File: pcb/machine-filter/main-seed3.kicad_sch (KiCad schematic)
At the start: 10 parts, among them J14 EXPANSION 2x4, J15 TF-01A

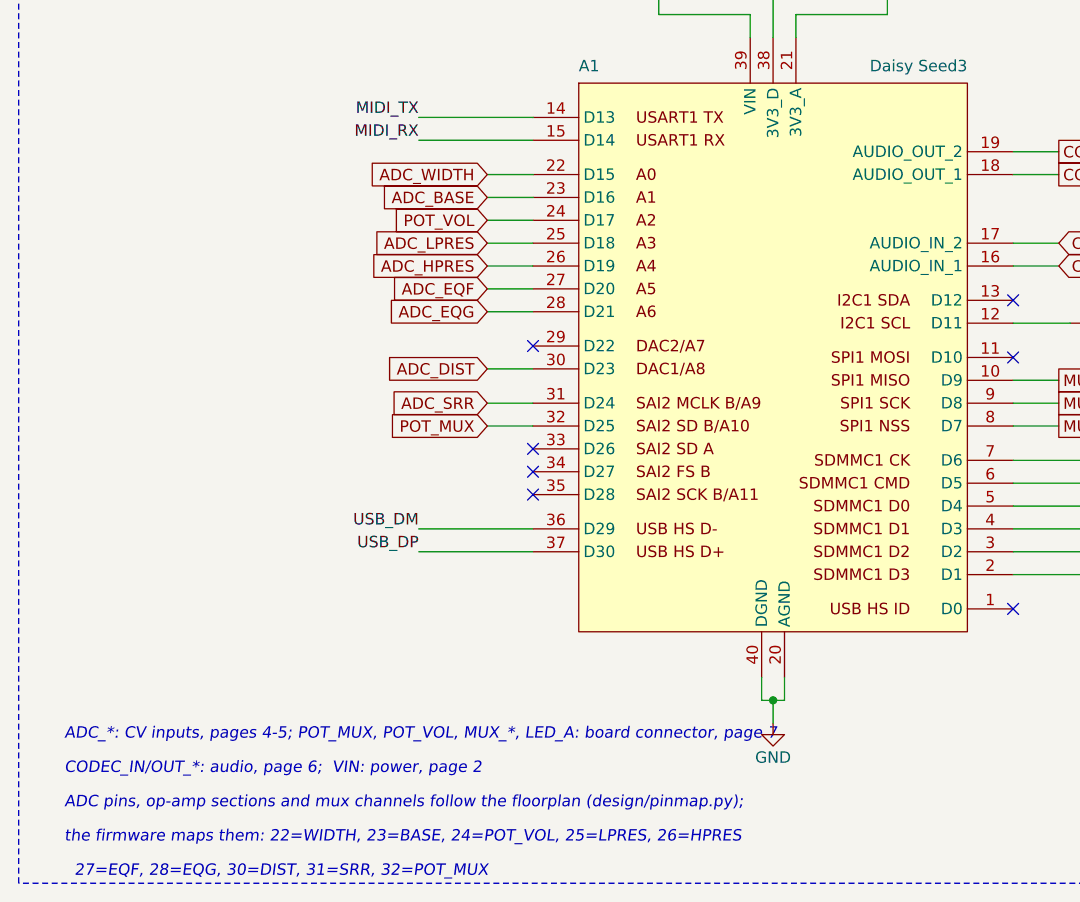
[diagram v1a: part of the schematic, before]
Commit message: Placement step 4: U1 and its CV group; ADC pins re-matched to the placed chips
Re-match pending d's OK (d questioned doing it now): tools/rematch_adc.py,
pinmap ADC_UNIT/SEED_ADC, schematic rebuilt, firmware and placement docs
updated, PCB pads reassigned (U1 re-added: its unit A moved sheets).
WIDTH trace not drawn yet.

Co-Authored-By: Claude Opus 5.5 <noreply@anthropic.com>
Claude-Session: https://claude.ai/code/session_01Cf5qNBi3oNHhbCjPHvswth
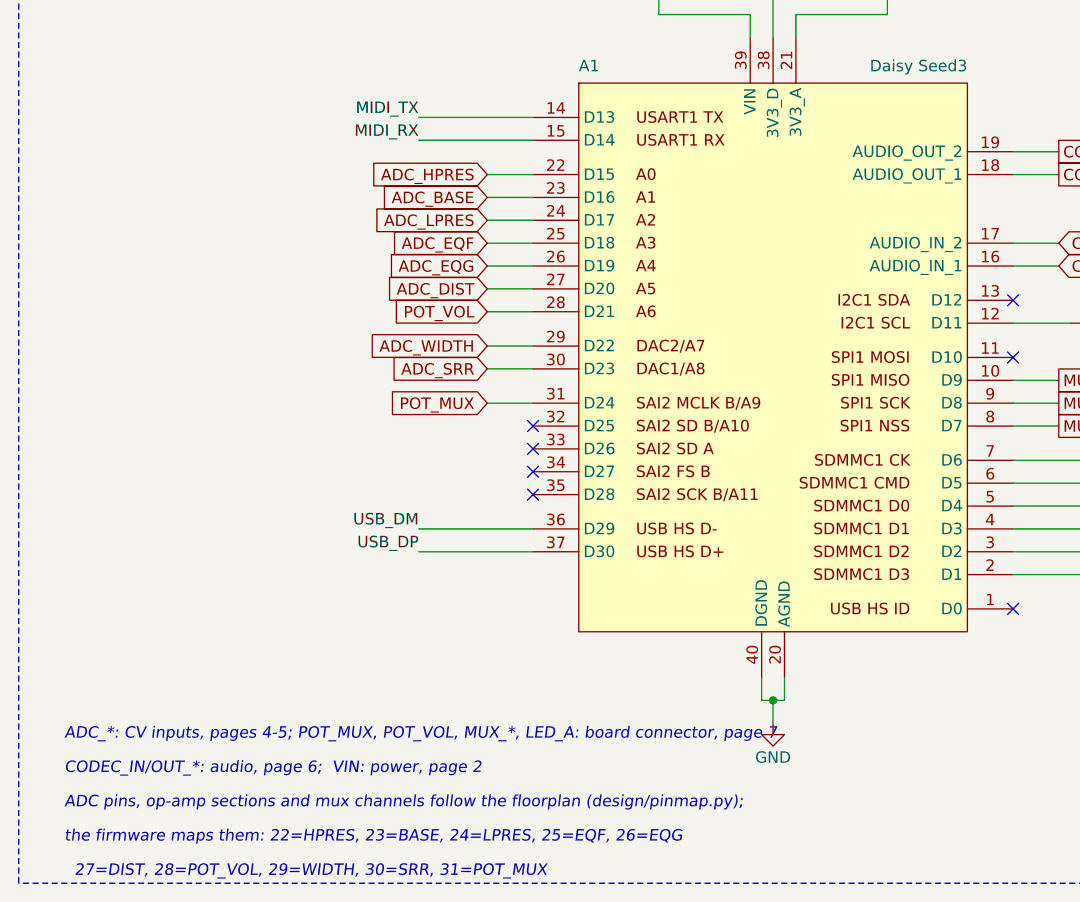
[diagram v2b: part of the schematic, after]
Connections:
- net ADC_DIST: now also A1.27 (D20); no longer A1.30 (D23)
- net ADC_EQF: now also A1.25 (D18); no longer A1.27 (D20)
- net ADC_EQG: now also A1.26 (D19); no longer A1.28 (D21)
- net ADC_HPRES: now also A1.22 (D15); no longer A1.26 (D19)
- net ADC_LPRES: now also A1.24 (D17); no longer A1.25 (D18)
- net ADC_SRR: now also A1.30 (D23); no longer A1.31 (D24)
- net ADC_WIDTH: now also A1.29 (D22); no longer A1.22 (D15)
- net POT_MUX: now also A1.31 (D24); no longer A1.32 (D25)
- net POT_VOL: now also A1.28 (D21); no longer A1.24 (D17)
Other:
- note added: "27=DIST, 28=POT_VOL, 29=WIDTH, 30=SRR, 31=POT_MUX"
- note added: "the firmware maps them: 22=HPRES, 23=BASE, 24=LPRES, 25=EQF, 26=EQG"
- note removed: "27=EQF, 28=EQG, 30=DIST, 31=SRR, 32=POT_MUX"
- note removed: "the firmware maps them: 22=WIDTH, 23=BASE, 24=POT_VOL, 25=LPRES, 26=HPRES"
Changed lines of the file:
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@@
 	)
 	(no_connect
-		(at 72.39 100.33)
+		(at 72.39 109.22)
 	)
 	(no_connect
@@
 		)
 	)
-	(global_label "ADC_WIDTH"
+	(global_label "ADC_HPRES"
 		(shape input)
 		(at 67.31 81.28 180)
@@
 		)
 	)
-	(global_label "POT_VOL"
+	(global_label "ADC_LPRES"
 		(shape input)
 		(at 67.31 86.36 180)
@@
 		)
 	)
-	(global_label "ADC_LPRES"
+	(global_label "ADC_EQF"
 		(shape input)
 		(at 67.31 88.9 180)
@@
 		)
 	)
-	(global_label "ADC_HPRES"
+	(global_label "ADC_EQG"
 		(shape input)
 		(at 67.31 91.44 180)
@@
 		)
 	)
-	(global_label "ADC_EQF"
+	(global_label "ADC_DIST"
 		(shape input)
 		(at 67.31 93.98 180)
@@
 		)
 	)
-	(global_label "ADC_EQG"
+	(global_label "POT_VOL"
 		(shape input)
 		(at 67.31 96.52 180)
@@
 		)
 	)
-	(global_label "ADC_DIST"
+	(global_label "ADC_WIDTH"
+		(shape input)
+		(at 67.31 100.33 180)
+		(fields_autoplaced yes)
+		(effects
+			(font
+				(size 1.27 1.27)
+			)
+			(justify right)
+		)
+		(property "Intersheetrefs" "${INTERSHEET_REFS}"
+			(at 67.31 100.33 180)
+			(effects
+				(font
+					(size 1.27 1.27)
+				)
+				(justify right)
+				(hide yes)
+			)
+		)
+	)
+	(global_label "ADC_SRR"
 		(shape input)
 		(at 67.31 102.87 180)
@@
 		)
 	)
-	(global_label "ADC_SRR"
+	(global_label "POT_MUX"
 		(shape input)
 		(at 67.31 106.68 180)
@@
 		(property "Intersheetrefs" "${INTERSHEET_REFS}"
 			(at 67.31 106.68 180)
-			(effects
-				(font
-					(size 1.27 1.27)
-				)
-				(justify right)
-				(hide yes)
-			)
-		)
-	)
-	(global_label "POT_MUX"
-		(shape input)
-		(at 67.31 109.22 180)
-		(fields_autoplaced yes)
-		(effects
-			(font
-				(size 1.27 1.27)
-			)
-			(justify right)
-		)
-		(property "Intersheetrefs" "${INTERSHEET_REFS}"
-			(at 67.31 109.22 180)
 			(effects
 				(font
@@
 		)
 	)
-	(text "the firmware maps them: 22=WIDTH, 23=BASE, 24=POT_VOL, 25=LPRES, 26=HPRES"
+	(text "the firmware maps them: 22=HPRES, 23=BASE, 24=LPRES, 25=EQF, 26=EQG"
 		(exclude_from_sim no)
 		(at 20.32 154.94 0)
@@
 		)
 	)
-	(text "  27=EQF, 28=EQG, 30=DIST, 31=SRR, 32=POT_MUX"
+	(text "  27=DIST, 28=POT_VOL, 29=WIDTH, 30=SRR, 31=POT_MUX"
 		(exclude_from_sim no)
 		(at 20.32 158.75 0)
@@
 	(wire
 		(pts
+			(xy 67.31 100.33)
+			(xy 72.39 100.33)
+		)
+		(stroke
+			(width 0)
+			(type default)
+		)
+	)
+	(wire
+		(pts
 			(xy 67.31 102.87)
 			(xy 72.39 102.87)
@@
 		)
 		(stroke
-			(width 0)
-			(type default)
-		)
-	)
-	(wire
-		(pts
-			(xy 67.31 109.22)
-			(xy 72.39 109.22)
-		)
-		(stroke

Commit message: Swap J14 pins 3 and 4 (USB_DP to pin 4, GND to pin 3); D+ straight on the front
The old D+ route squeezed between J14 pins 2 and 4 with 0.27 mm each side on a hand-soldered header (d, 2026-10-07).
Both sources, check_netlist EXPECTED, design-review and placement-guide updated; board updated from the schematic
(Konnect, 2 pads reassigned). DRC 0; candidate c04-j14-swap.

Co-Authored-By: Claude Opus 5.5 <noreply@anthropic.com>
Claude-Session: https://claude.ai/code/session_01Cf5qNBi3oNHhbCjPHvswth
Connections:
- net GND: now also J14.3 (Pin_3); no longer J14.4 (Pin_4)
- net USB_DP: now also J14.4 (Pin_4); no longer J14.3 (Pin_3)
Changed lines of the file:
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@@
-		)
-	)
-	(label "USB_DP"
-		(at 218.44 68.58 180)
-		(effects
-			(font
-				(size 1.27 1.27)
-			)
-			(justify right bottom)
 		)
 	)
 	(symbol
 		(lib_id "power:GND")
-		(at 254 68.58 90)
+		(at 231.14 68.58 270)
 		(unit 1)
 		(exclude_from_sim no)
@@
 		(dnp no)
 		(property "Reference" "#PWR019"
-			(at 260.35 68.58 90)
+			(at 224.79 68.58 90)
 			(effects
 				(font
@@
 		)
 		(property "Value" "GND"
-			(at 257.3 68.58 90)
+			(at 227.84 68.58 90)
 			(effects
 				(font
@@
 		)
 		(property "Footprint" ""
-			(at 254 68.58 90)
+			(at 231.14 68.58 90)
 			(effects
 				(font
@@
 		)
 		(property "Datasheet" ""
-			(at 254 68.58 90)
+			(at 231.14 68.58 90)
 			(effects
 				(font
@@
 		)
 		(property "Description" "Power symbol creates a global label with name \"GND\" , ground"
-			(at 254 68.58 90)
+			(at 231.14 68.58 90)
 			(effects
 				(font
@@
 		)
 	)
+	(label "USB_DP"
+		(at 266.7 68.58 0)
+		(effects
+			(font
+				(size 1.27 1.27)
+			)
+			(justify left bottom)
+		)
+	)
 	(label "MIDI_TX"
 		(at 218.44 71.12 180)
@@
 	(wire
 		(pts
-			(xy 218.44 68.58)
+			(xy 231.14 68.58)
 			(xy 236.22 68.58)
 		)
@@
 		(pts
 			(xy 248.92 68.58)
-			(xy 254 68.58)
-		)
-		(stroke
+			(xy 266.7 68.58)
+		)
+		(stroke
